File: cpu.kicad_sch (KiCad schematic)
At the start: 22 parts, among them IC1 68HC000, IC2 LHP6323, IC7 MSM54C864

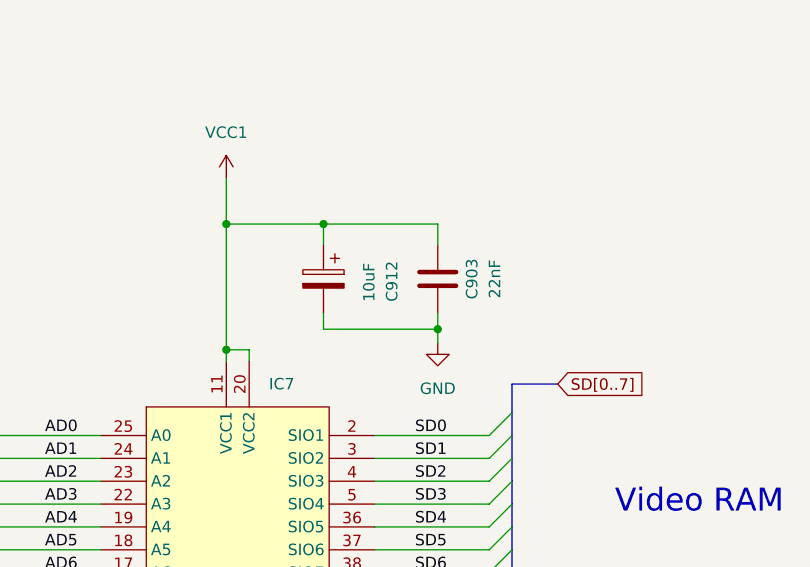
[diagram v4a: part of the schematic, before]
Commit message: Add RGB amp from 3BP.
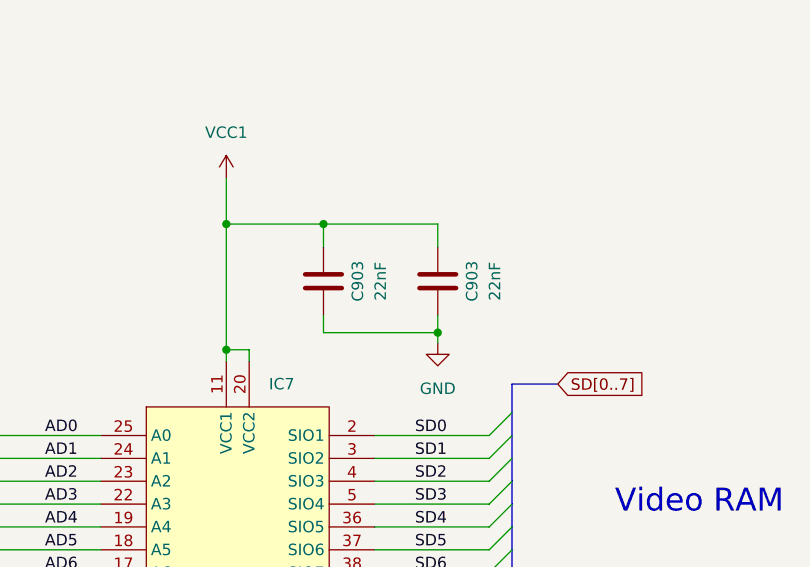
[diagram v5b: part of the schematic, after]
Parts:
- removed C912: 10uF, Neptune:CP_Radial_D5.0mm_P2.50mm_Horizontal, symbol Device:C_Polarized
- added C903: 22nF, Capacitor_SMD:C_0805_2012Metric, symbol Device:C
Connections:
- net GND: now also C903.1
- net VCC1: now also C903.2
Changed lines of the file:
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@@
   (junction (at 143.51 241.3) (diameter 0) (color 0 0 0 0)
   )
-  (junction (at 323.85 161.544) (diameter 0) (color 0 0 0 0)
-  )
   (junction (at 102.87 241.3) (diameter 0) (color 0 0 0 0)
   )
@@
   (junction (at 250.825 49.53) (diameter 0) (color 0 0 0 0)
   )
+  (junction (at 311.15 149.86) (diameter 0) (color 0 0 0 0)
+  )
   (junction (at 118.11 241.3) (diameter 0) (color 0 0 0 0)
   )
@@
   (junction (at 158.115 241.3) (diameter 0) (color 0 0 0 0)
   )
+  (junction (at 323.85 161.925) (diameter 0) (color 0 0 0 0)
+  )
   (junction (at 125.73 241.3) (diameter 0) (color 0 0 0 0)
   )
@@
   (junction (at 300.355 149.86) (diameter 0) (color 0 0 0 0)
   )
-  (junction (at 311.15 149.86) (diameter 0) (color 0 0 0 0)
-  )
   (junction (at 163.83 47.625) (diameter 0) (color 0 0 0 0)
   )
@@
     (stroke (width 0) (type default))
   )
-  (wire (pts (xy 323.85 161.544) (xy 323.85 163.068))
-    (stroke (width 0) (type default))
-  )
   (bus (pts (xy 203.2 67.31) (xy 203.2 64.77))
     (stroke (width 0) (type default))
@@
     (stroke (width 0) (type default))
   )
+  (wire (pts (xy 323.85 161.925) (xy 311.15 161.925))
+    (stroke (width 0) (type default))
+  )
   (wire (pts (xy 295.91 57.15) (xy 295.91 49.53))
     (stroke (width 0) (type default))
@@
     (stroke (width 0) (type default))
   )
-  (wire (pts (xy 311.15 149.86) (xy 311.15 152.146))
-    (stroke (width 0) (type default))
-  )
   (bus (pts (xy 203.2 92.71) (xy 203.2 90.17))
     (stroke (width 0) (type default))
@@
     (stroke (width 0) (type default))
   )
+  (wire (pts (xy 323.85 160.02) (xy 323.85 161.925))
+    (stroke (width 0) (type default))
+  )
   (wire (pts (xy 65.405 241.3) (xy 65.405 234.95))
     (stroke (width 0) (type default))
@@
     (stroke (width 0) (type default))
   )
-  (wire (pts (xy 323.85 152.146) (xy 323.85 149.86))
+  (wire (pts (xy 323.85 152.4) (xy 323.85 149.86))
     (stroke (width 0) (type default))
   )
@@
     (stroke (width 0) (type default))
   )
-  (wire (pts (xy 323.85 149.86) (xy 311.15 149.86))
+  (wire (pts (xy 300.355 149.86) (xy 311.15 149.86))
     (stroke (width 0) (type default))
   )
@@
     (stroke (width 0) (type default))
   )
+  (wire (pts (xy 311.15 149.86) (xy 311.15 152.4))
+    (stroke (width 0) (type default))
+  )
   (wire (pts (xy 127 82.55) (xy 140.97 82.55))
     (stroke (width 0) (type default))
@@
     (stroke (width 0) (type default))
   )
+  (wire (pts (xy 323.85 161.925) (xy 323.85 163.068))
+    (stroke (width 0) (type default))
+  )
   (wire (pts (xy 160.655 214.63) (xy 160.655 226.06))
     (stroke (width 0) (type default))
@@
     (stroke (width 0) (type default))
   )
-  (wire (pts (xy 311.15 161.544) (xy 323.85 161.544))
-    (stroke (width 0) (type default))
-  )
   (wire (pts (xy 102.87 214.63) (xy 102.87 226.06))
     (stroke (width 0) (type default))
   )
-  (wire (pts (xy 300.355 149.86) (xy 311.15 149.86))
-    (stroke (width 0) (type default))
-  )
   (bus (pts (xy 272.415 186.055) (xy 272.415 188.595))
     (stroke (width 0) (type default))
@@
     (stroke (width 0) (type default))
   )
-  (wire (pts (xy 323.85 159.766) (xy 323.85 161.544))
-    (stroke (width 0) (type default))
-  )
   (bus (pts (xy 220.98 62.23) (xy 220.98 59.69))
     (stroke (width 0) (type default))
@@
     (stroke (width 0) (type default))
   )
-  (wire (pts (xy 311.15 159.766) (xy 311.15 161.544))
-    (stroke (width 0) (type default))
-  )
   (bus (pts (xy 135.89 212.09) (xy 123.19 212.09))
     (stroke (width 0) (type default))
@@
     (stroke (width 0) (type default))
   )
+  (wire (pts (xy 311.15 149.86) (xy 323.85 149.86))
+    (stroke (width 0) (type default))
+  )
   (bus (pts (xy 277.495 85.09) (xy 277.495 82.55))
     (stroke (width 0) (type default))
@@
     (stroke (width 0) (type default))
   )
+  (wire (pts (xy 311.15 161.925) (xy 311.15 160.02))
+    (stroke (width 0) (type default))
+  )
   (wire (pts (xy 316.865 212.09) (xy 320.675 212.09))
     (stroke (width 0) (type default))
@@
     )
   )
-  (symbol (lib_id "Device:C") (at 323.85 155.956 0) (mirror x) (unit 1)
+  (symbol (lib_id "Device:C") (at 323.85 156.21 0) (mirror x) (unit 1)
     (in_bom yes) (on_board yes) (dnp no)
-    (property "Reference" "C903" (at 327.66 155.956 90)
+    (property "Reference" "C903" (at 327.66 156.21 90)
       (effects (font (size 1.27 1.27)))
     )
-    (property "Value" "22nF" (at 330.2 155.956 90)
+    (property "Value" "22nF" (at 330.2 156.21 90)
       (effects (font (size 1.27 1.27)))
     )
-    (property "Footprint" "Capacitor_SMD:C_0805_2012Metric" (at 324.8152 152.146 0)
+    (property "Footprint" "Capacitor_SMD:C_0805_2012Metric" (at 324.8152 152.4 0)
       (effects (font (size 1.27 1.27)) hide)
     )
-    (property "Datasheet" "~" (at 323.85 155.956 0)
+    (property "Datasheet" "~" (at 323.85 156.21 0)
       (effects (font (size 1.27 1.27)) hide)
     )
-    (property "DigiKey" "" (at 323.85 155.956 0)
+    (property "DigiKey" "" (at 323.85 156.21 0)
       (effects (font (size 1.27 1.27)) hide)
     )
@@
     )
   )
-  (symbol (lib_id "Device:C_Polarized") (at 311.15 155.956 0) (mirror y) (unit 1)
-    (in_bom yes) (on_board yes) (dnp no)
-    (property "Reference" "C912" (at 318.77 158.496 90)
-      (effects (font (size 1.27 1.27)) (justify left))
-    )
-    (property "Value" "10uF" (at 316.23 158.496 90)
-      (effects (font (size 1.27 1.27)) (justify left))
-    )
-    (property "Footprint" "Neptune:CP_Radial_D5.0mm_P2.50mm_Horizontal" (at 310.1848 159.766 0)
-      (effects (font (size 1.27 1.27)) hide)
-    )
-    (property "Datasheet" "~" (at 311.15 155.956 0)
-      (effects (font (size 1.27 1.27)) hide)
-    )
-    (property "DigiKey" "" (at 311.15 155.956 0)
-      (effects (font (size 1.27 1.27)) hide)
-    )
-    (pin "1")
-    (pin "2")
-    (instances
-      (project "Neptune"
-        (path "/bcc23b51-b742-4ae5-9dd6-d96a24058944/01513199-62c5-4123-a151-ccd381a5e6c1"
-          (reference "C912") (unit 1)
-        )
-        (path "/bcc23b51-b742-4ae5-9dd6-d96a24058944/293c8f1f-2c58-4557-aeb8-8502bb66fbd4"
-          (reference "CE21") (unit 1)
-        )
-        (path "/bcc23b51-b742-4ae5-9dd6-d96a24058944/48e60f61-77cc-4ea0-898f-0029aa970ca5"
-          (reference "CE22") (unit 1)
-        )
-      )
-    )
-  )
   (symbol (lib_id "MegaDrive:C_Pack04") (at 123.19 231.14 0) (unit 1)
     (in_bom yes) (on_board yes) (dnp no)
@@
         )
       )
+    )
+  )
+  (symbol (lib_id "Device:C") (at 311.15 156.21 0) (mirror x) (unit 1)
+    (in_bom yes) (on_board yes) (dnp no)
+    (property "Reference" "C903" (at 314.96 156.21 90)
+      (effects (font (size 1.27 1.27)))
+    )
+    (property "Value" "22nF" (at 317.5 156.21 90)
+      (effects (font (size 1.27 1.27)))
+    )
+    (property "Footprint" "Capacitor_SMD:C_0805_2012Metric" (at 312.1152 152.4 0)
+      (effects (font (size 1.27 1.27)) hide)
+    )
+    (property "Datasheet" "~" (at 311.15 156.21 0)
+      (effects (font (size 1.27 1.27)) hide)
+    )
+    (property "DigiKey" "" (at 311.15 156.21 0)
+      (effects (font (size 1.27 1.27)) hide)
+    )
+    (pin "1")
+    (pin "2")
+    (instances
+      (project "Neptune"
+        (path "/bcc23b51-b742-4ae5-9dd6-d96a24058944/01513199-62c5-4123-a151-ccd381a5e6c1"
+          (reference "C903") (unit 1)
+        )
+        (path "/bcc23b51-b742-4ae5-9dd6-d96a24058944/293c8f1f-2c58-4557-aeb8-8502bb66fbd4"
+          (reference "C41") (unit 1)
+        )
+        (path "/bcc23b51-b742-4ae5-9dd6-d96a24058944/48e60f61-77cc-4ea0-898f-0029aa970ca5"
+          (reference "C642") (unit 1)
+        )
+      )

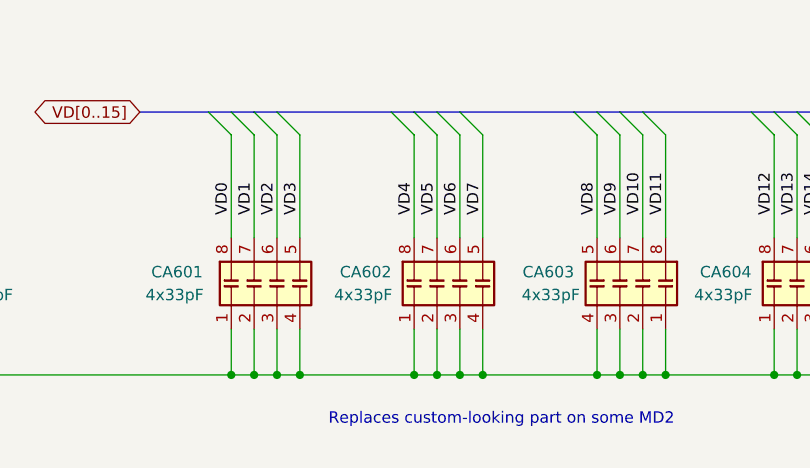
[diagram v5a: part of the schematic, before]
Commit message: Remove mono audio, switch to 2-unit opamp.
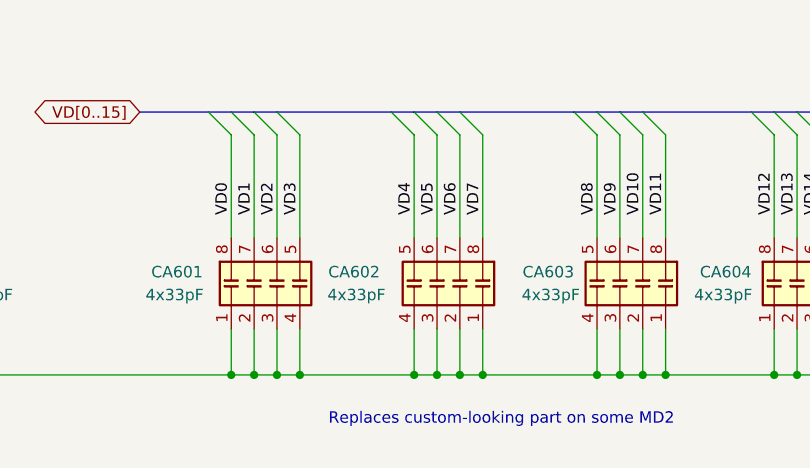
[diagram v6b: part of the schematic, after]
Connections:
- net VD4: now also CA602.5 (R4.2); no longer CA602.8 (R1.2)
- net VD5: now also CA602.6 (R3.2); no longer CA602.7 (R2.2)
- net VD6: now also CA602.7 (R2.2); no longer CA602.6 (R3.2)
- net VD7: now also CA602.8 (R1.2); no longer CA602.5 (R4.2)
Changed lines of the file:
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@@
     )
   )
-  (symbol (lib_id "MegaDrive:C_Pack04") (at 123.19 231.14 0) (unit 1)
+  (symbol (lib_id "MegaDrive:C_Pack04") (at 120.65 231.14 0) (mirror y) (unit 1)
     (in_bom yes) (on_board yes) (dnp no)
-    (property "Reference" "CA602" (at 109.855 229.87 0)
+    (property "Reference" "CA602" (at 114.3 229.87 0)
       (effects (font (size 1.27 1.27)) (justify left))
     )
-    (property "Value" "4x33pF" (at 109.22 232.41 0)
+    (property "Value" "4x33pF" (at 114.935 232.41 0)
       (effects (font (size 1.27 1.27)) (justify left))
     )
-    (property "Footprint" "Resistor_SMD:R_Array_Convex_4x0603" (at 130.175 231.14 90)
+    (property "Footprint" "Resistor_SMD:R_Array_Convex_4x0603" (at 113.665 231.14 90)
       (effects (font (size 1.27 1.27)) hide)
     )
@@
       (effects (font (size 1.27 1.27)) hide)
     )
-    (property "DigiKey" "13-CA0612KRNPO9BN330CT-ND" (at 123.19 231.14 0)
+    (property "DigiKey" "13-CA0612KRNPO9BN330CT-ND" (at 120.65 231.14 0)
       (effects (font (size 1.27 1.27)) hide)
     )

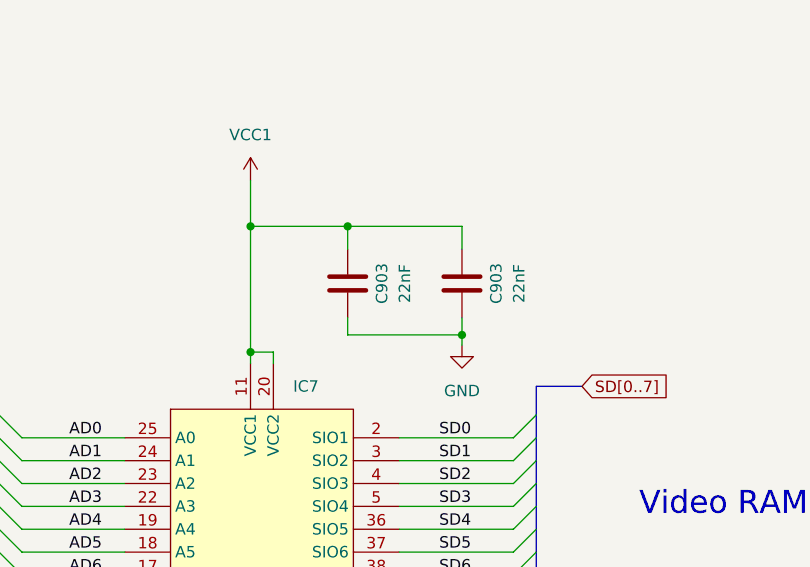
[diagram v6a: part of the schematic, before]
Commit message: Footprint improvements, general tidying.
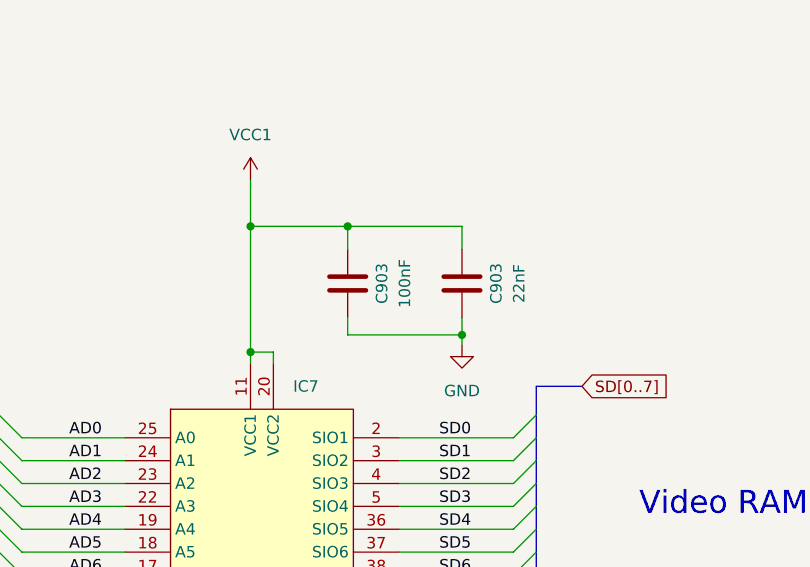
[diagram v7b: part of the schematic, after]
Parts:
- C903: value 22nF -> 100nF
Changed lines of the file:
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@@
       (effects (font (size 1.27 1.27)))
     )
-    (property "Value" "22nF" (at 317.5 156.21 90)
+    (property "Value" "100nF" (at 317.5 156.21 90)
       (effects (font (size 1.27 1.27)))
     )

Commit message: Added LCSC Part # for some of the bird seed
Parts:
- C16, C18, C3, C5: LCSC Part # (none) -> C2232364
- C17, C2: LCSC Part # (none) -> C2232461
- C903: LCSC Part # (none) -> C2224419
- C903: LCSC Part # (none) -> C2237864
- CA601, CA602, CA603, CA604: LCSC Part # (none) -> C576634
- FB7: LCSC Part # (none) -> C2441367
- R3: LCSC Part # (none) -> C844204
- R3: LCSC Part # (none) -> C313835
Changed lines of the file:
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@@
+      (effects (font (size 1.27 1.27)) hide)
+    )
+    (property "LCSC Part #" "C576634" (at 140.97 231.14 0)
       (effects (font (size 1.27 1.27)) hide)
     )
@@
       (effects (font (size 1.27 1.27)) hide)
     )
+    (property "LCSC Part #" "C2224419" (at 323.85 156.21 0)
+      (effects (font (size 1.27 1.27)) hide)
+    )
     (pin "1")
     (pin "2")
@@
     )
     (property "DigiKey" "" (at 166.37 115.57 0)
+      (effects (font (size 1.27 1.27)) hide)
+    )
+    (property "LCSC Part #" "" (at 166.37 115.57 0)
       (effects (font (size 1.27 1.27)) hide)
     )
@@
       (effects (font (size 1.27 1.27)) hide)
     )
+    (property "LCSC Part #" "C2232461" (at 65.405 231.14 0)
+      (effects (font (size 1.27 1.27)) hide)
+    )
     (pin "1")
     (pin "2")
@@
     )
     (property "DigiKey" "" (at 301.625 193.675 0)
+      (effects (font (size 1.27 1.27)) hide)
+    )
+    (property "LCSC Part #" "" (at 301.625 193.675 0)
       (effects (font (size 1.27 1.27)) hide)
     )
@@
       (effects (font (size 1.27 1.27)) hide)
     )
+    (property "LCSC Part #" "C2232461" (at 349.885 216.535 0)
+      (effects (font (size 1.27 1.27)) hide)
+    )
     (pin "1")
     (pin "2")
@@
       (effects (font (size 1.27 1.27)) hide)
     )
+    (property "LCSC Part #" "C844204" (at 196.85 163.83 0)
+      (effects (font (size 1.27 1.27)) hide)
+    )
     (pin "1")
     (pin "2")
@@
     )
     (property "DigiKey" "" (at 333.375 216.535 0)
+      (effects (font (size 1.27 1.27)) hide)
+    )
+    (property "LCSC Part #" "" (at 333.375 216.535 0)
       (effects (font (size 1.27 1.27)) hide)
     )
@@
     )
     (property "DigiKey" "13-CA0612KRNPO9BN330CT-ND" (at 102.87 231.14 0)
+      (effects (font (size 1.27 1.27)) hide)
+    )
+    (property "LCSC Part #" "C576634" (at 102.87 231.14 0)
       (effects (font (size 1.27 1.27)) hide)
     )
@@
       (effects (font (size 1.27 1.27)) hide)
     )
+    (property "LCSC Part #" "C313835" (at 135.255 133.35 0)
+      (effects (font (size 1.27 1.27)) hide)
+    )
     (pin "1")
     (pin "2")
@@
       (effects (font (size 1.27 1.27)) hide)
     )
+    (property "LCSC Part #" "C2232364" (at 358.14 216.535 0)
+      (effects (font (size 1.27 1.27)) hide)
+    )
     (pin "1")
     (pin "2")
@@
     )
     (property "DigiKey" "" (at 295.91 60.96 0)
+      (effects (font (size 1.27 1.27)) hide)
+    )
+    (property "LCSC Part #" "C2224419" (at 295.91 60.96 0)
       (effects (font (size 1.27 1.27)) hide)
     )
@@
       (effects (font (size 1.27 1.27)) hide)
     )
+    (property "LCSC Part #" "C2232364" (at 341.63 216.535 0)
+      (effects (font (size 1.27 1.27)) hide)
+    )
     (pin "1")
     (pin "2")
@@
     )
     (property "DigiKey" "13-CA0612KRNPO9BN330CT-ND" (at 120.65 231.14 0)
+      (effects (font (size 1.27 1.27)) hide)
+    )
+    (property "LCSC Part #" "C576634" (at 120.65 231.14 0)
       (effects (font (size 1.27 1.27)) hide)
     )
@@
       (effects (font (size 1.27 1.27)) hide)
     )
+    (property "LCSC Part #" "C2232364" (at 271.145 111.76 0)
+      (effects (font (size 1.27 1.27)) hide)
+    )
     (pin "1")
     (pin "2")
@@
     )
     (property "DigiKey" "13-CA0612KRNPO9BN330CT-ND" (at 163.195 231.14 0)
+      (effects (font (size 1.27 1.27)) hide)
+    )
+    (property "LCSC Part #" "C576634" (at 163.195 231.14 0)
       (effects (font (size 1.27 1.27)) hide)
     )
@@
       (effects (font (size 1.27 1.27)) hide)
     )
+    (property "LCSC Part #" "C2232364" (at 285.115 111.76 0)
+      (effects (font (size 1.27 1.27)) hide)
+    )
     (pin "1")
     (pin "2")
@@
     )
     (property "DigiKey" "" (at 249.555 76.835 0)
+      (effects (font (size 1.27 1.27)) hide)
+    )
+    (property "LCSC Part #" "" (at 249.555 76.835 0)
       (effects (font (size 1.27 1.27)) hide)
     )
@@
       (effects (font (size 1.27 1.27)) hide)
     )
+    (property "LCSC Part #" "C2441367" (at 135.255 59.69 0)
+      (effects (font (size 1.27 1.27)) hide)
+    )
     (pin "1")
     (pin "2")
@@
       (effects (font (size 1.27 1.27)) hide)
     )
+    (property "LCSC Part #" "" (at 102.235 55.88 0)
+      (effects (font (size 1.27 1.27)) hide)
+    )
     (pin "1")
     (pin "2")
@@
       (effects (font (size 1.27 1.27)) hide)
     )
+    (property "LCSC Part #" "C2237864" (at 311.15 156.21 0)
+      (effects (font (size 1.27 1.27)) hide)
+    )
     (pin "1")
     (pin "2")
@@
       (effects (font (size 1.27 1.27)) hide)
     )
+    (property "LCSC Part #" "C2224419" (at 89.535 55.88 0)
+      (effects (font (size 1.27 1.27)) hide)
+    )
